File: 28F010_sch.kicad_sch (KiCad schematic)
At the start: 12 parts, among them U10 74LVC1G332, U11 74LS138, U12 CY7C199, U15 CY7C199, U16 4012, U17 CY7C199, U8 74LS138, U9 CY7C199

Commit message: Added the databus
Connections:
- net D0: now reaches Bank0.13 (DQ0)
- net D0: now also Bank1.13 (DQ0), U12.11 (D0), U15.11 (D0), U17.11 (D0), U9.11 (D0)
- net D1: now reaches Bank0.14 (DQ1)
- net D1: now also Bank1.14 (DQ1), U12.12 (D1), U15.12 (D1), U17.12 (D1), U9.12 (D1)
- net D2: now reaches Bank0.15 (DQ2)
- net D2: now also Bank1.15 (DQ2), U12.13 (D2), U15.13 (D2), U17.13 (D2), U9.13 (D2)
- net D3: now reaches Bank0.17 (DQ3)
- net D3: now also Bank1.17 (DQ3), U12.15 (D3), U15.15 (D3), U17.15 (D3), U9.15 (D3)
- net D4: now reaches Bank0.18 (DQ4)
- net D4: now also Bank1.18 (DQ4), U12.16 (D4), U15.16 (D4), U17.16 (D4), U9.16 (D4)
- net D5: now reaches Bank0.19 (DQ5)
- net D5: now also Bank1.19 (DQ5), U12.17 (D5), U15.17 (D5), U17.17 (D5), U9.17 (D5)
- net D6: now reaches Bank0.20 (DQ6)
- net D6: now also Bank1.20 (DQ6), U12.18 (D6), U15.18 (D6), U17.18 (D6), U9.18 (D6)
- net D7: now reaches Bank0.21 (DQ7)
- net D7: now also Bank1.21 (DQ7), U12.19 (D7), U15.19 (D7), U17.19 (D7), U9.19 (D7)
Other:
- moved on the sheet: U9

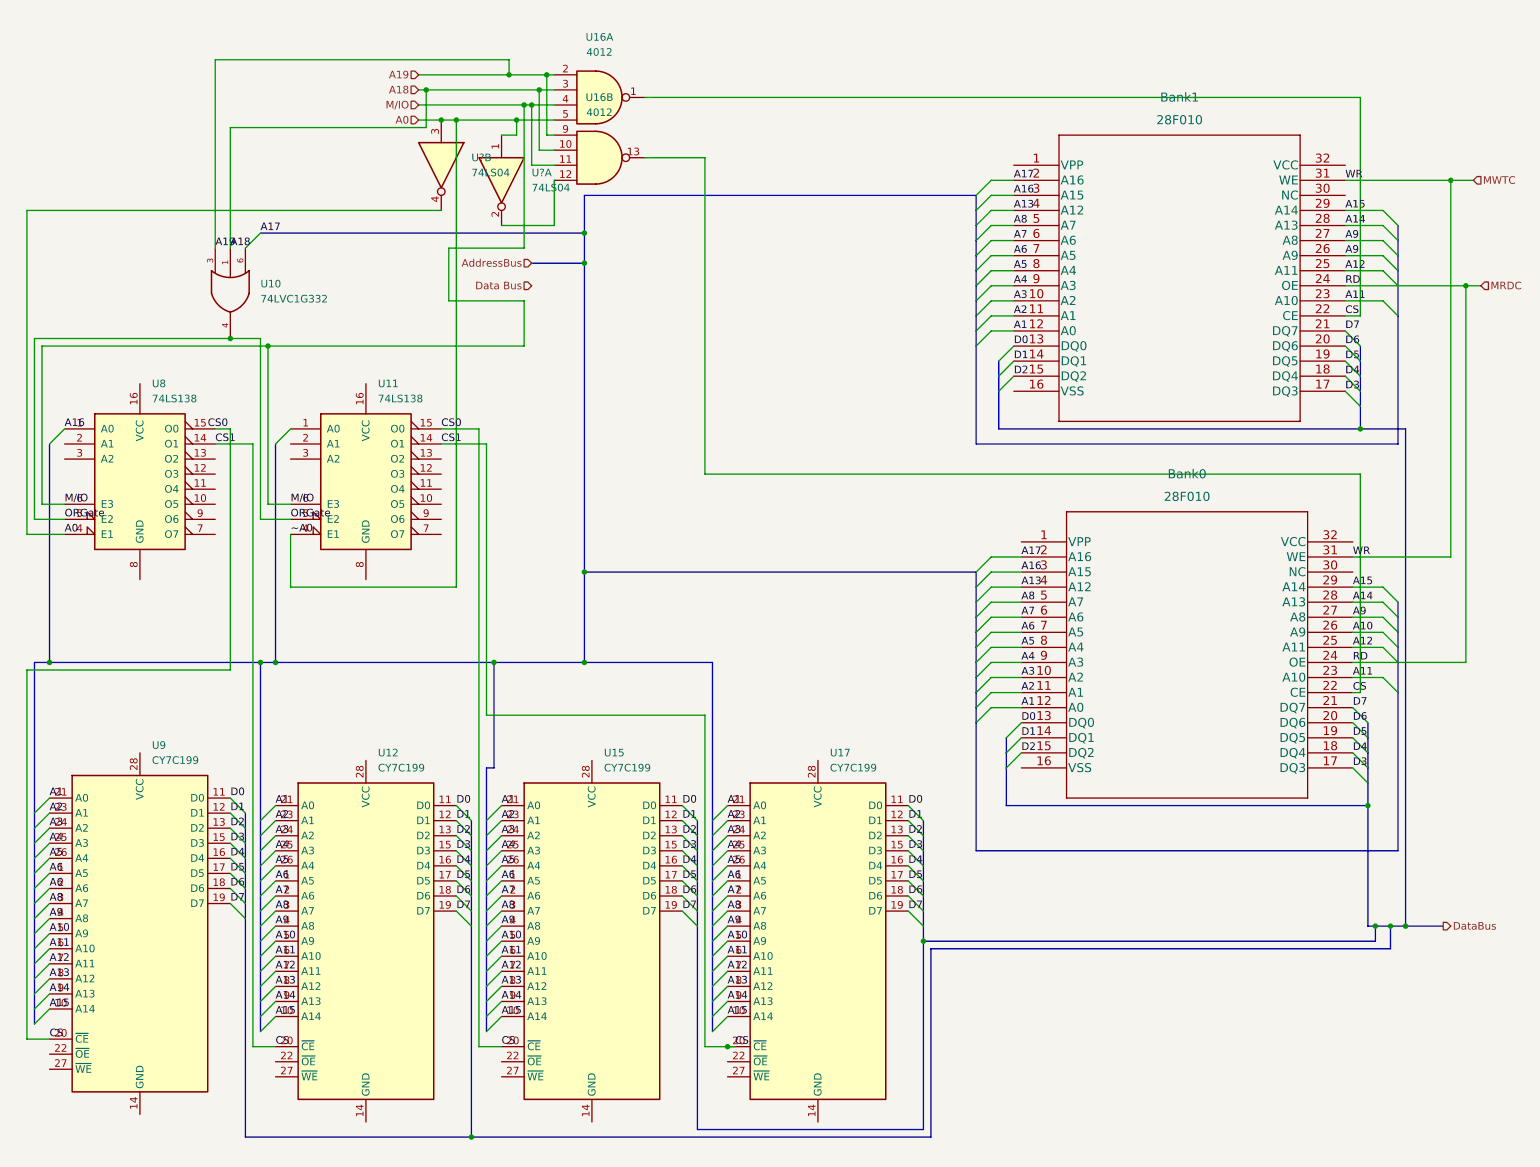
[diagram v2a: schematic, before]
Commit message: Finished wiring and decoding IO devices (except for push button switches)
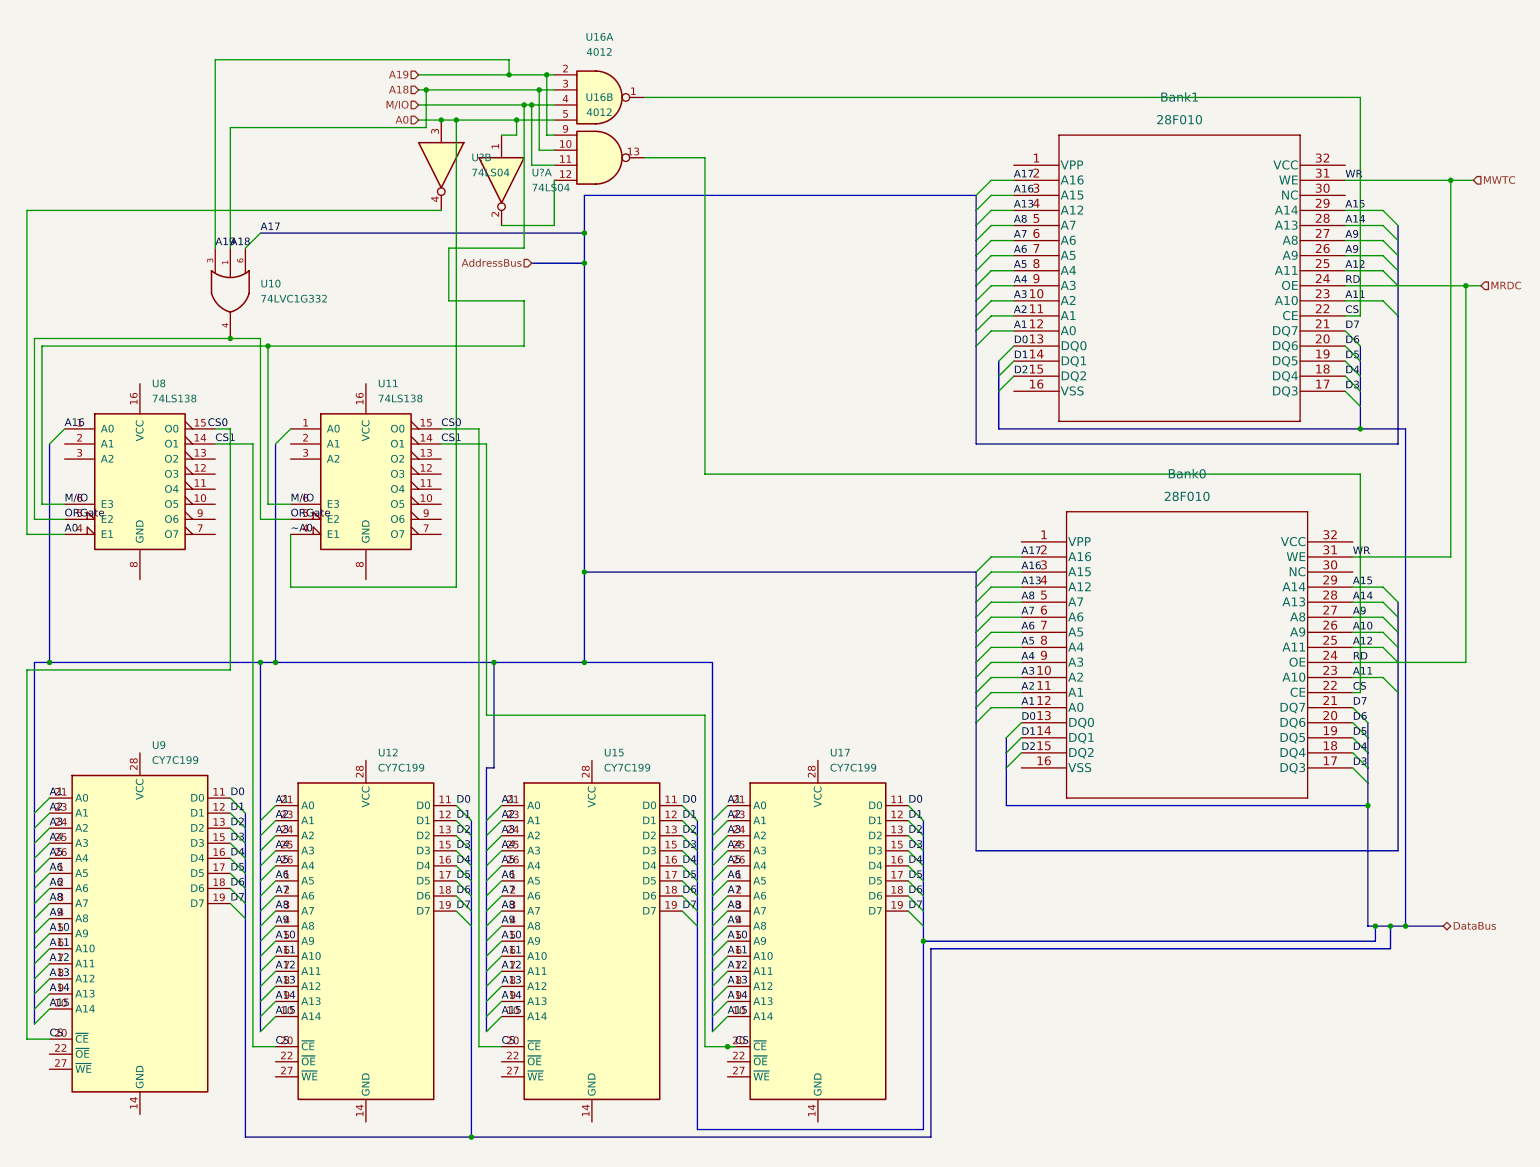
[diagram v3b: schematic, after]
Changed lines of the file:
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@@
     (effects (font (size 1.27 1.27)) (justify right))
   )
-  (hierarchical_label "DataBus" (shape output) (at 254 158.75 0)
+  (hierarchical_label "DataBus" (shape bidirectional) (at 254 158.75 0)
     (effects (font (size 1.27 1.27)) (justify left))
   )
@@
     (effects (font (size 1.27 1.27)) (justify right))
   )
-  (hierarchical_label "Data Bus" (shape input) (at 100.33 50.8 180)
-    (effects (font (size 1.27 1.27)) (justify right))
-  )

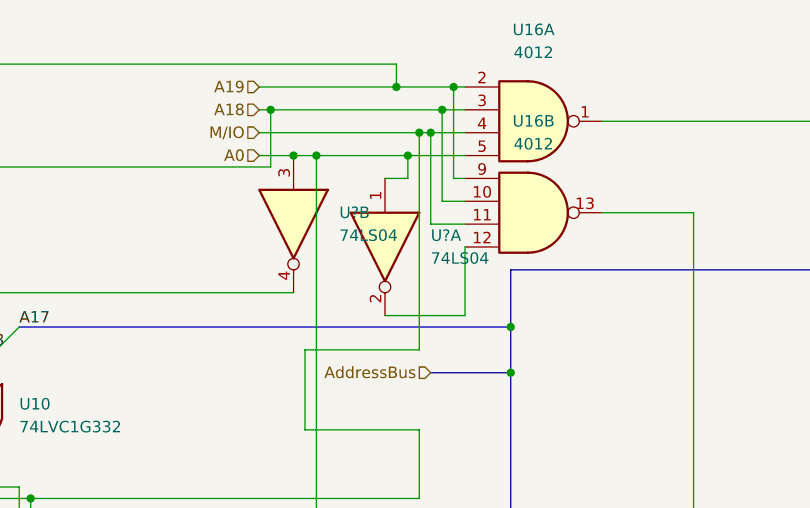
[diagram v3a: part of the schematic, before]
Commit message: Wired Push Buttons and added footprints
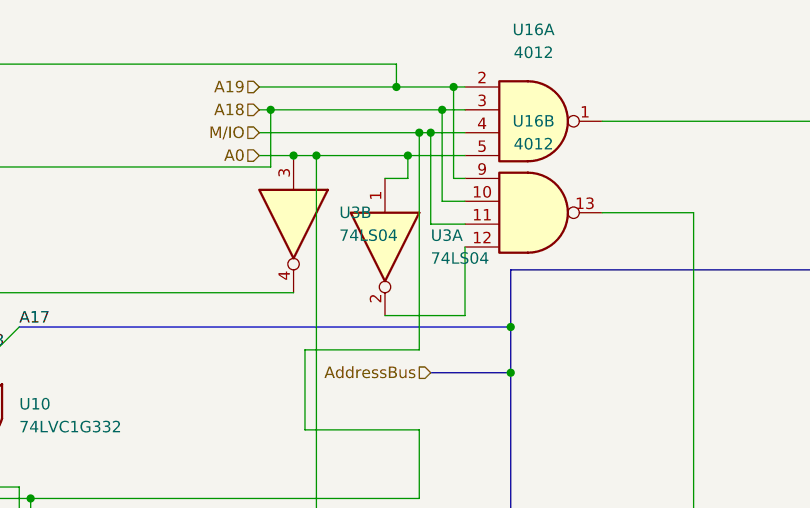
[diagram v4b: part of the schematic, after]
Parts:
- gave numbers to parts that had none: 1
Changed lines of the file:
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@@
   (symbol (lib_id "74xx:74LS04") (at 85.09 30.48 270) (unit 2)
     (in_bom yes) (on_board yes) (fields_autoplaced)
-    (property "Reference" "U?" (id 0) (at 90.17 29.2099 90)
+    (property "Reference" "U3" (id 0) (at 90.17 29.2099 90)
       (effects (font (size 1.27 1.27)) (justify left))
     )
@@
   (symbol (lib_id "74xx:74LS04") (at 95.25 33.02 270) (unit 1)
     (in_bom yes) (on_board yes) (fields_autoplaced)
-    (property "Reference" "U?" (id 0) (at 100.33 31.7499 90)
-      (effects (font (size 1.27 1.27)) (justify left))
-    )
+    (property "Reference" "U3" (id 0) (at 100.33 31.7499 90)
+      (effects (font (size 1.27 1.27)) (justify left))
+    )

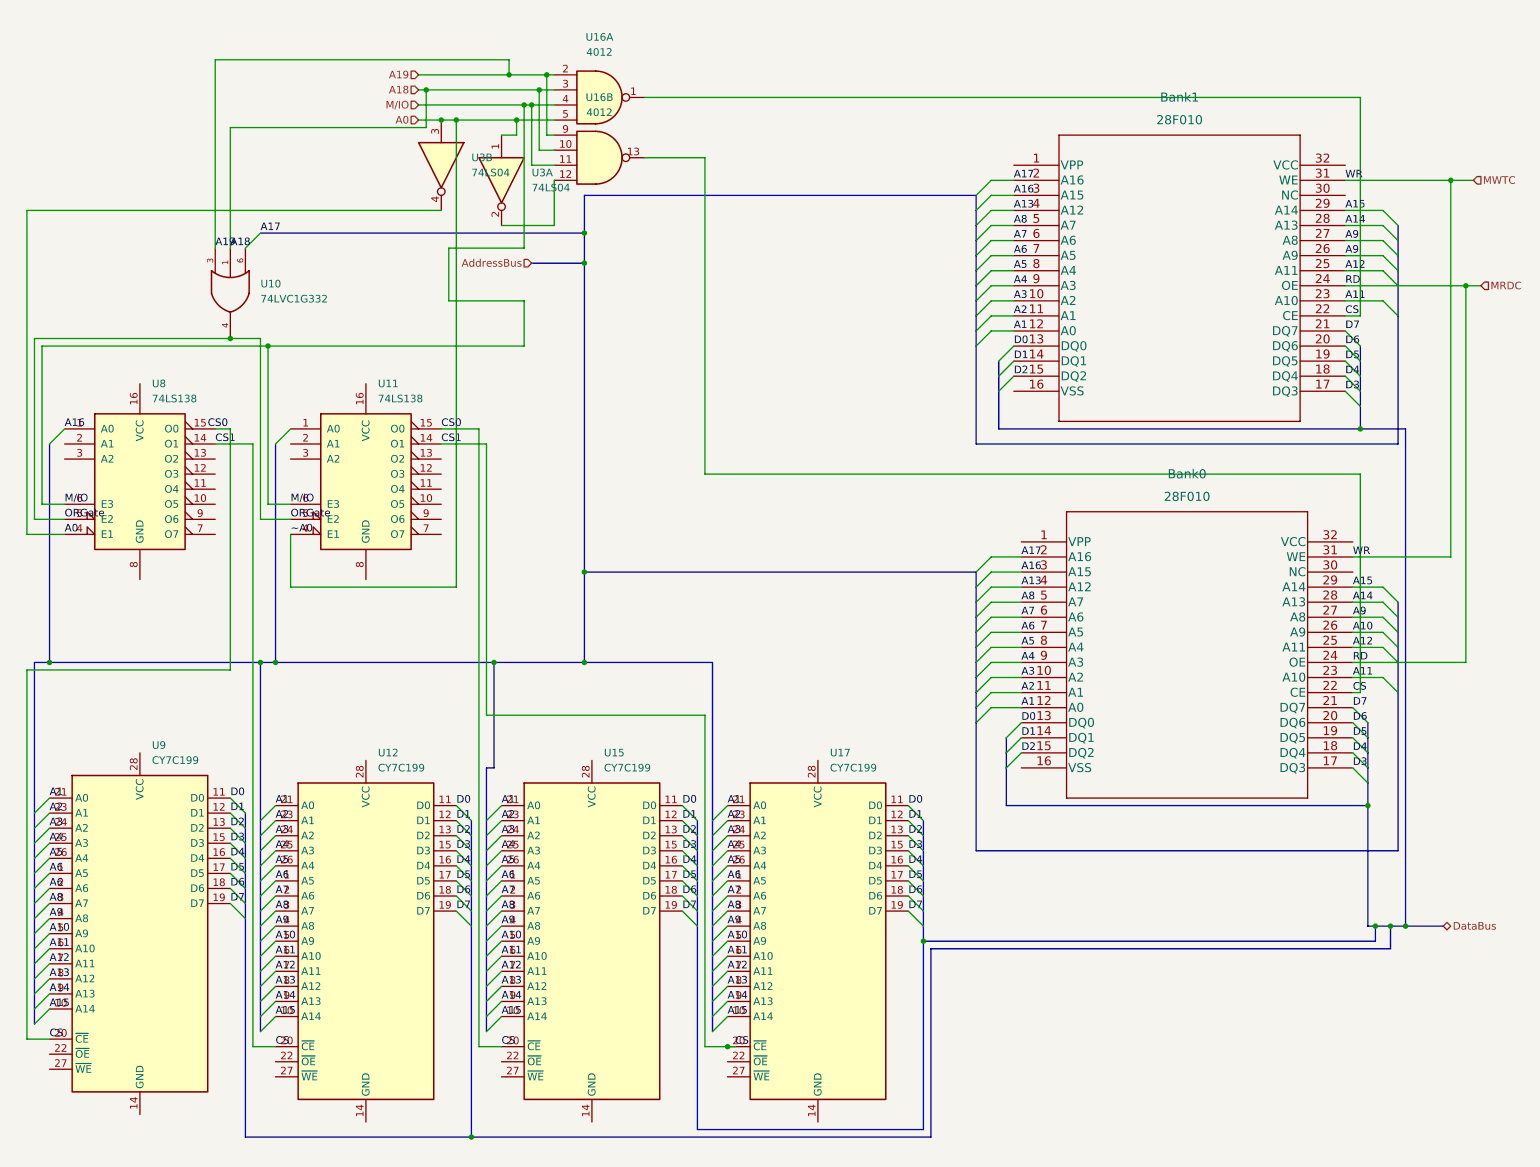
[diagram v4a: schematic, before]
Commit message: Added power and ground to chips
Added power and ground to chips as well as checked and added all labels for pins off of busses
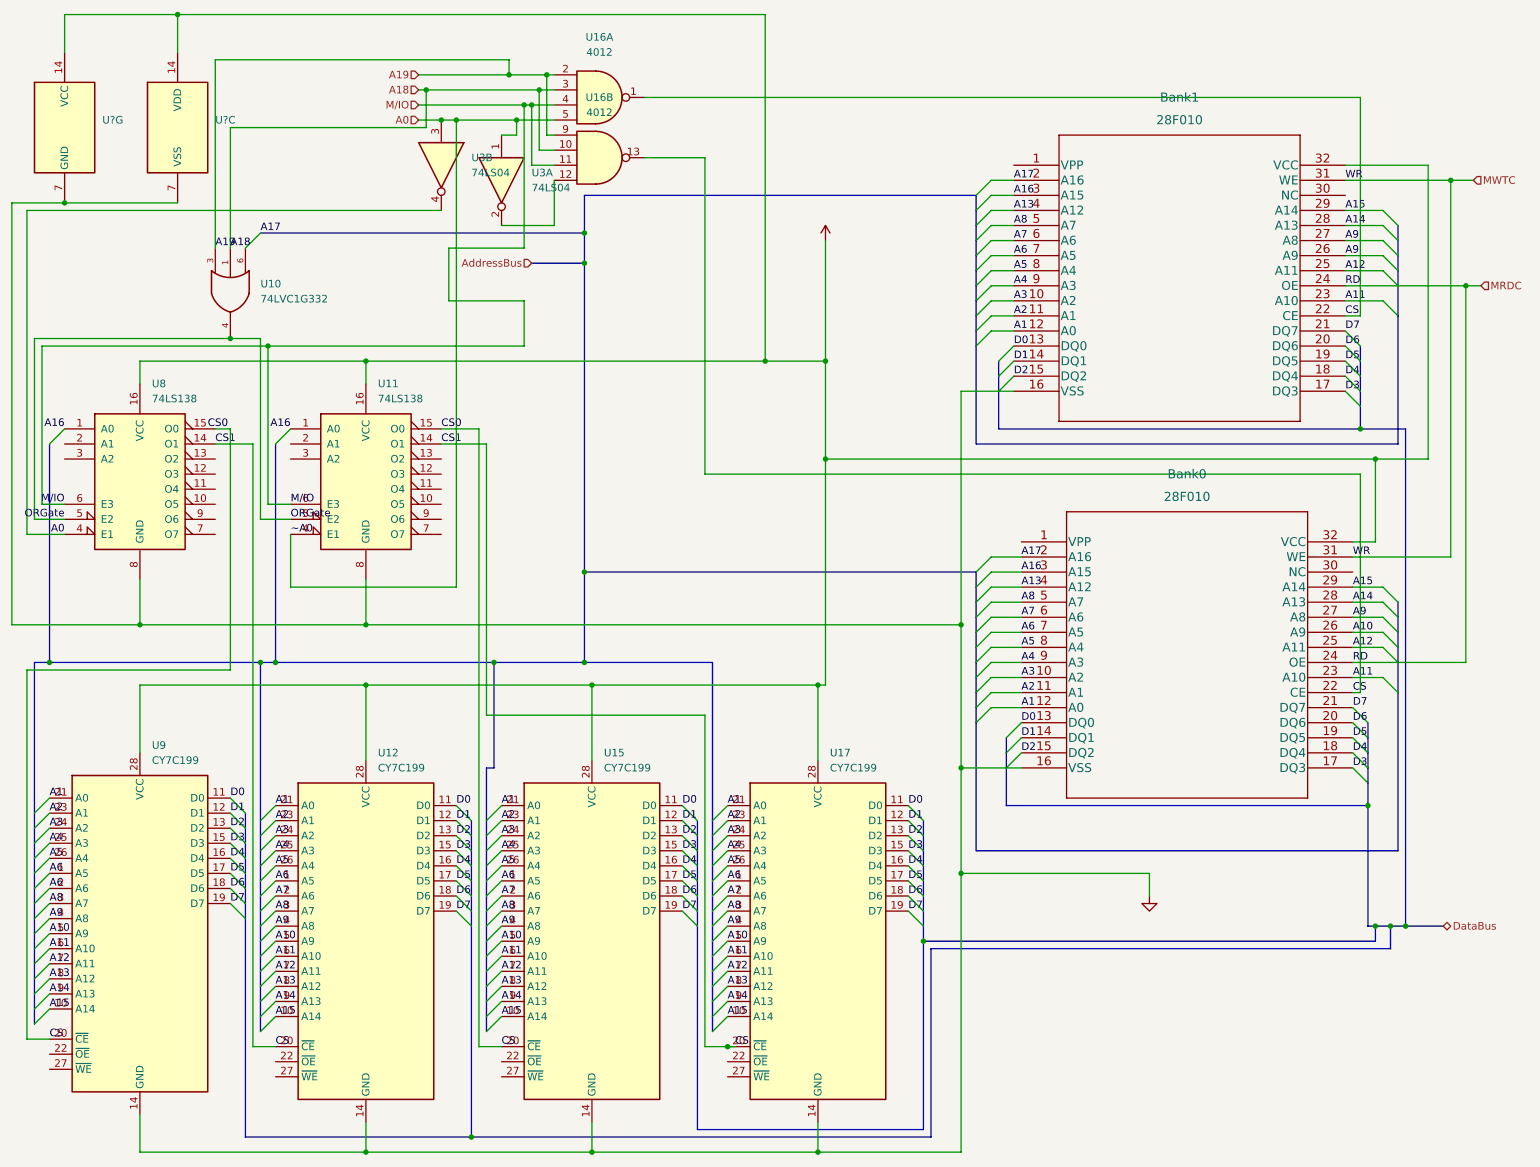
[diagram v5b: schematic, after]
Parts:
- added U?: (no value), symbol 74xx:74LS04
- added U?: (no value), symbol 4xxx:4012
- U10: footprint (none) -> Package_TO_SOT_SMD:SOT-23-6
- U11, U8: footprint (none) -> Package_DIP:DIP-16_W7.62mm
- U12, U15, U17, U9: footprint (none) -> Package_DIP:DIP-28_W7.62mm
- U16: footprint (none) -> Package_DIP:DIP-12_W7.62mm
- U3: footprint (none) -> Package_DIP:DIP-14_W7.62mm
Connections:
- net A16: now also U11.1 (A0)
- net GND: now also Bank0.16 (VSS), Bank1.16 (VSS), U11.8 (GND), U12.14 (GND), U15.14 (GND), U17.14 (GND), U8.8 (GND), U9.14 (GND), U?.7 (GND), U?.7 (VSS)
- net +5V: now reaches Bank0.32 (VCC)
- net +5V: now also Bank1.32 (VCC), U11.16 (VCC), U12.28 (VCC), U15.28 (VCC), U17.28 (VCC), U8.16 (VCC), U9.28 (VCC), U?.14 (VCC), U?.14 (VDD)
